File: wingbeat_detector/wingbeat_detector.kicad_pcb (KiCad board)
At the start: 4 copper layers, 36 x 18 mm, 54 parts, among them J1 USB_C_10137062-00021LF, J2 UMC_JACK_SMD, J3 UMC_JACK_SMD, J4 UMC_JACK_SMD, Q1 MOSFET-N-CH, U1 MAX865EUA+, U2 UAF42_SMA, U3 UAF42_SMA, U4 OPA381, U5 TSV630IQ1T, U6 LED_DRV_50mA

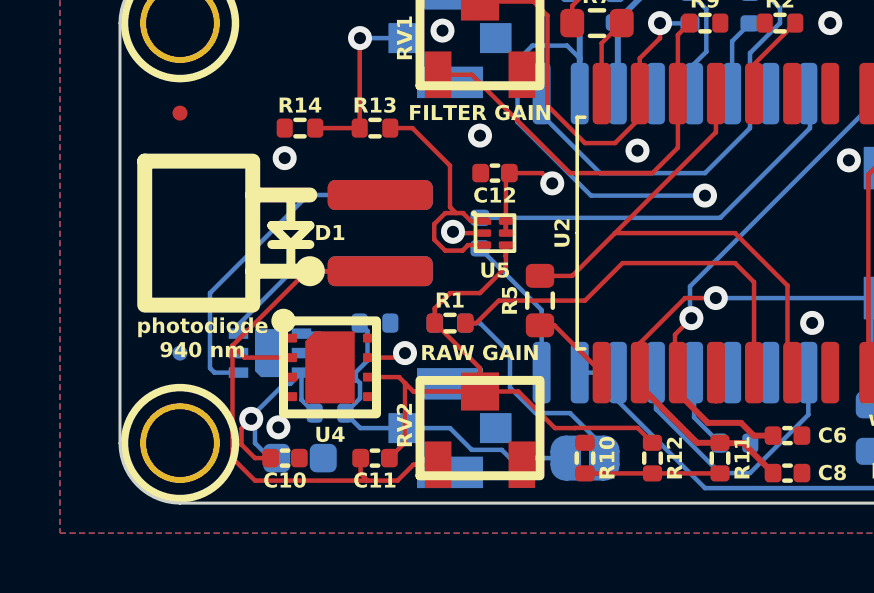
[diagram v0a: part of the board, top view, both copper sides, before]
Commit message: Remove LED
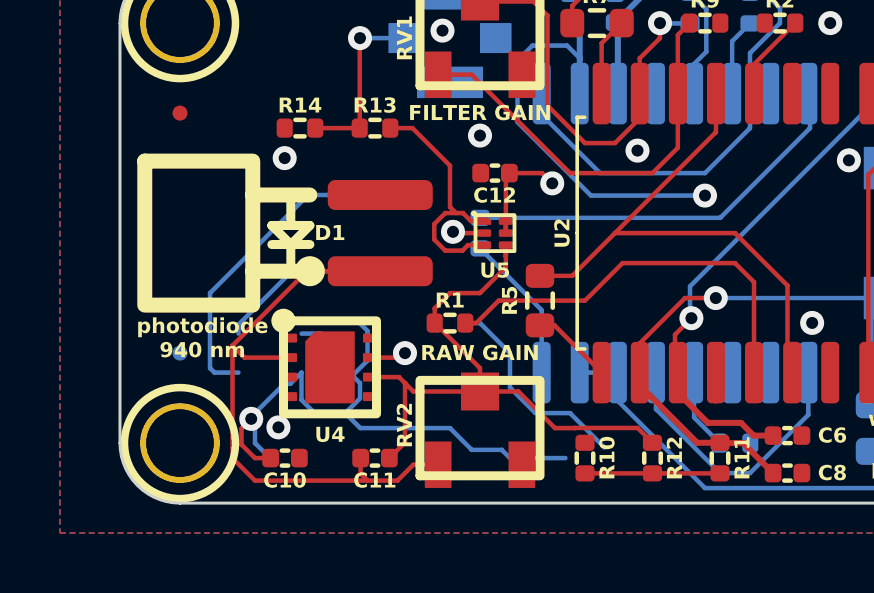
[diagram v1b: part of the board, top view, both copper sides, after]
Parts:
- removed C13: 4.7uF, Janelia:C_0603_1608Metric
- removed D2: LED, Janelia:LED_RADIAL_RA_SMD_BRIGHT
- removed J4: UMC_JACK_SMD, Janelia:UMC_AMPHENOL_A-1JB
- removed JP1: SolderJumper_2_Open, Janelia:SolderJumper-2_P1.3mm_Open_RoundedPad1.0x1.5mm
- removed Q1: MOSFET-N-CH, Janelia:XFDFN-3
- removed R15: 23.2k, Janelia:R_0402_1005Metric
- removed R16: 49.9k, Janelia:R_0402_1005Metric
- removed R17: 2k, Janelia:R_0402_1005Metric
- removed U6: LED_DRV_50mA, Janelia:DFN-6-1EP_2x2mm_P0.65mm_EP1x1.6mm
- H1, H2, H3, H4: value VAL** -> MOUNTING_HOLE_2
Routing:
- net (no net): track 0.00 -> 35.6 mm
- net /led/LED_ENABLE: track 11.5 -> 0.00 mm
- net Net-(D2-A): track 9.49 -> 0.00 mm
- net Net-(JP1-A): track 7.03 -> 0.00 mm
- net Net-(D2-K): track 5.76 -> 0.00 mm
- net /led/VB: track 1.79 -> 0.00 mm
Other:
- board text removed: "JUMP LED DEFAULT DISABLED"
- board text removed: "LED 940 nm"
- board text removed: "LED ENABLE"

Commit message: More progress towards v4
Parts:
- removed C12: 0.1uF, Janelia:C_0402_1005Metric
- removed J3: UMC_JACK_SMD, Janelia:UMC_AMPHENOL_A-1JB
- removed RV1, RV2: 500k, Janelia:Potentiometer_Bourns_3223W_Vertical
- removed U5: TSV630IQ1T, Janelia:PSON40P120X130X50-6N
- C10, C11, R11, R12, U4: moved to B.Cu
- R10: value 49.9k -> GAIN1; footprint Janelia:R_0402_1005Metric -> Janelia:R_1206_3216Metric
- R13: value 23.2k -> 49.9k; moved to B.Cu
- R14: value 49.9k -> GAIN0; footprint Janelia:R_0402_1005Metric -> Janelia:R_1206_3216Metric; moved to B.Cu
- moved R10 29.0 mm to (172.0, 92.0), turned to 180 degrees
- moved R8 17.5 mm to (155.8, 113.0)
- moved C11 13.3 mm to (139.5, 94.2)
- moved R1 13.0 mm to (142.5, 116.0)
- moved R11 12.9 mm to (139.2, 105.5), turned to 0 degrees
- moved FID1 12.1 mm to (139.0, 107.0)
- moved R5 10.9 mm to (148.8, 112.8)
- moved R12 8.49 mm to (141.5, 105.5), turned to 0 degrees
- moved R13 7.32 mm to (141.5, 103.8), turned to 0 degrees
- moved FID4 5.83 mm to (139.0, 107.0)
- moved C10 5.15 mm to (139.5, 102.8), turned to 180 degrees
- moved U4 4.50 mm to (139.5, 100.0)
- moved C1 2.00 mm to (156.0, 93.5)
- moved C2 2.00 mm to (160.0, 106.5)
- moved C3 2.00 mm to (157.5, 106.5)
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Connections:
- R10 pad 1: /GND -> Net-(U2-AAin-)
- R10 pad 2: Net-(R10-Pad2) -> /filter/HIGHPASS_AMPLIFIED
- R11 pad 1: Net-(R10-Pad2) -> /GND
- R11 pad 2: /V10- -> Net-(R11-Pad2)
- R12 pad 1: Net-(R10-Pad2) -> Net-(R11-Pad2)
- R12 pad 2: /PHOTODIODE_RAW -> /V10-
- R13 pad 1: /photodiode/PHOTODIODE_BUFFERED -> Net-(R11-Pad2)
- R13 pad 2: /photodiode/PHOTODIODE_BUFFERED_SCALED -> /PHOTODIODE_RAW
- R14 pad 1: /photodiode/PHOTODIODE_BUFFERED_SCALED -> Net-(D1-K)
- R14 pad 2: /GND -> /PHOTODIODE_RAW
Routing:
- net /V10+: track 45.3 -> 0.00 mm, vias 1 -> 0
- net /V10-: track 36.0 -> 0.00 mm, vias 2 -> 0
- net (no net): track 35.6 -> 0.00 mm
- net /filter/BANDPASS_BUFFERED: track 25.8 -> 0.00 mm
- net Net-(U2-Fadj2): track 24.5 -> 0.00 mm
- net /V5+: track 20.9 -> 0.00 mm, vias 4 -> 0
- net /PHOTODIODE_RAW: track 20.4 -> 0.00 mm
- net /filter/HIGHPASS: track 18.2 -> 0.00 mm
- net Net-(U2-AAin-): track 14.0 -> 0.00 mm
- net Net-(U3-Fadj1): track 14.0 -> 0.00 mm
- net Net-(U2-Vin1): track 13.7 -> 0.00 mm
- net Net-(U3-Fadj2): track 13.3 -> 0.00 mm
- net /filter/HIGHPASS_AMPLIFIED: track 13.0 -> 0.00 mm, vias 1 -> 0
- net Net-(D1-K): track 18.4 -> 6.29 mm, vias 0 -> 1
- net /filter/LOWPASS: track 9.39 -> 0.00 mm
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- removed copper zone on B.Cu, net /GND
- removed copper zone on F.Cu, net /GND
- removed copper zone on In1.Cu, net /GND
- removed copper zone on In2.Cu, net /V5+
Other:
- board size 36 x 18 mm -> 32 x 18 mm
- board text added: "wingbeat detector v4.0 12/2023 peter@polidoro.io"
- board text removed: "RAW OUTPUT"
- board text removed: "wingbeat detector v3.2 03/2023 peter@polidoro.io"

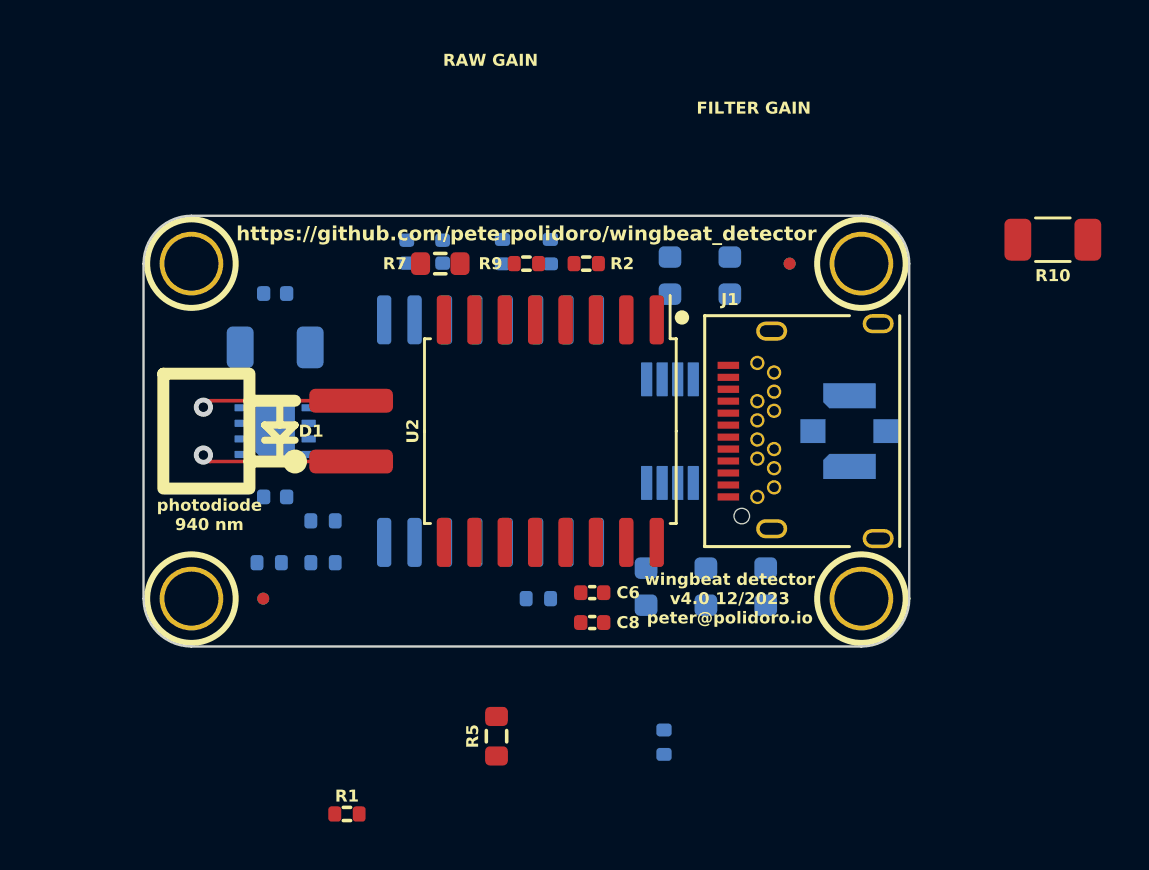
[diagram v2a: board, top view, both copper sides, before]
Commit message: First attempt at routing
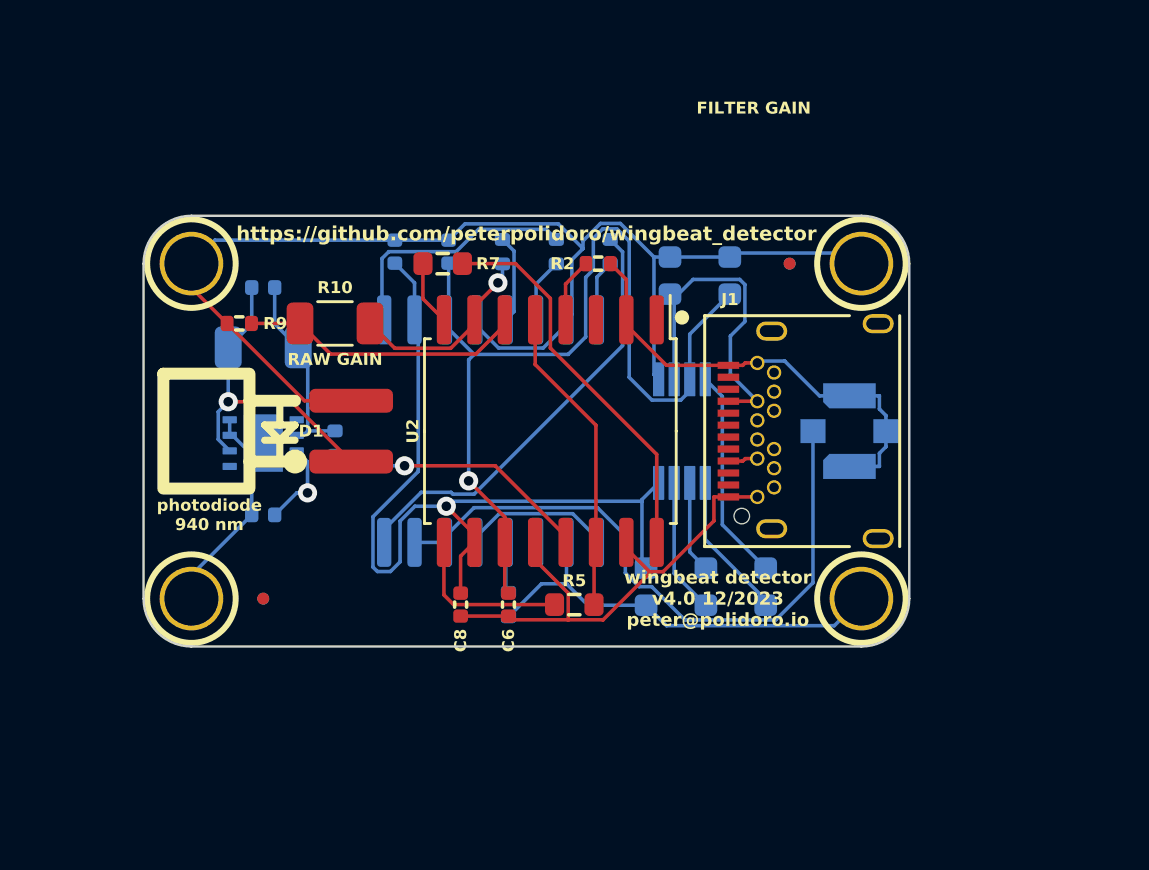
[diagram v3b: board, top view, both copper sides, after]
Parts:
- removed R12, R13: 49.9k, Janelia:R_0402_1005Metric
- removed R14: GAIN0, Janelia:R_1206_3216Metric
- C10: value 0.1uF -> 1uF
- C11: value 2pF -> 30pF
- R1: moved to B.Cu
- R11: value 49.9k -> 2M; footprint Janelia:R_0402_1005Metric -> Janelia:R_1206_3216Metric
- moved R10 30.2 mm to (142.0, 95.5), turned to 0 degrees
- moved R8 20.6 mm to (153.5, 92.5), turned to -90 degrees
- moved R1 15.5 mm to (142.0, 100.5), turned to -90 degrees
- moved R9 12.3 mm to (138.0, 95.5), turned to 180 degrees
- moved R11 9.00 mm to (139.0, 96.5)
- moved R5 6.39 mm to (152.0, 107.2), turned to 180 degrees
- moved C8 5.55 mm to (147.2, 107.2), turned to 90 degrees
- moved C6 3.54 mm to (149.2, 107.2), turned to -90 degrees
- moved R4 1.27 mm to (149.2, 107.2), turned to -90 degrees
- moved C10 0.90 mm to (139.0, 103.5)
- moved U4 0.71 mm to (139.0, 100.5)
- moved C11 0.56 mm to (139.0, 94.0)
- moved C9 0.50 mm to (144.5, 92.5)
- moved R2 0.50 mm to (153.0, 93.0), turned to 0 degrees
- moved U1 0.50 mm to (156.5, 100.0)
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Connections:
- R11 pad 1: /GND -> Net-(D1-K)
- R11 pad 2: Net-(R11-Pad2) -> /PHOTODIODE_RAW
- U4 pad 1: (no net) -> unconnected-(U4-NC-Pad1)
- U4 pad 5: (no net) -> unconnected-(U4-NC-Pad5)
- U4 pad 8: (no net) -> unconnected-(U4-NC-Pad8)
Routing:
- net /GND: track 6.29 -> 154.0 mm, vias 1 -> 0
- net /V5+: track 0.00 -> 41.1 mm, vias 0 -> 1
- net /V10+: track 0.00 -> 39.8 mm, vias 0 -> 1
- net /V10-: track 0.00 -> 35.7 mm, vias 0 -> 1
- net /filter/BANDPASS_BUFFERED: track 0.00 -> 27.2 mm
- net Net-(U3-BPVo): track 0.00 -> 18.4 mm
- net Net-(U2-Fadj2): track 0.00 -> 16.3 mm
- net /filter/HIGHPASS: track 0.00 -> 13.0 mm
- net Net-(U2-AAin-): track 0.00 -> 11.8 mm
- net Net-(U2-Vin1): track 0.00 -> 11.3 mm, vias 0 -> 1
- net Net-(U3-Fadj1): track 0.00 -> 10.6 mm
- net /power/C1+: track 0.00 -> 8.94 mm
- net /PHOTODIODE_RAW: track 0.00 -> 8.24 mm
- net /filter/HIGHPASS_AMPLIFIED: track 0.00 -> 8.23 mm, vias 0 -> 1
- net Net-(D1-K): track 6.29 -> 13.8 mm
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
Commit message: Adjust tracks and zones
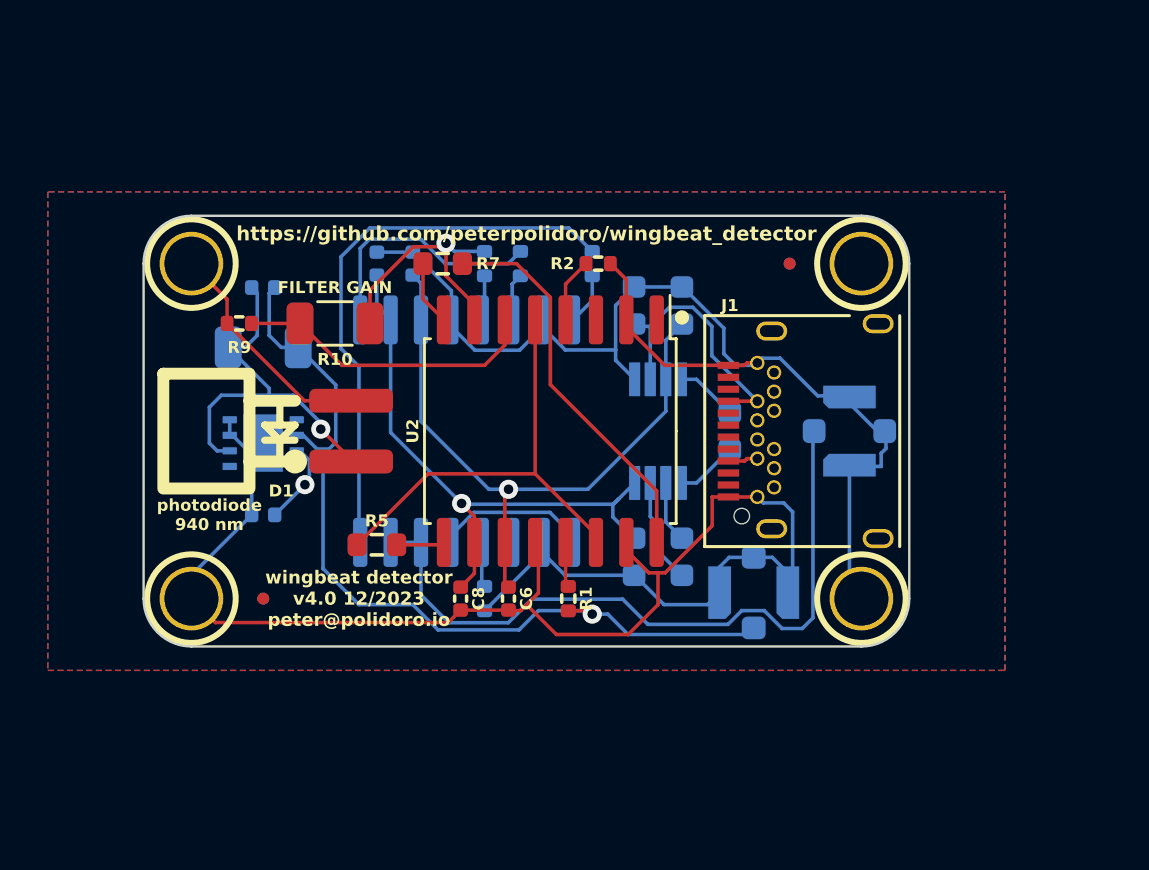
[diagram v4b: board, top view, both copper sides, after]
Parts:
- added J3: UMC_JACK_SMD, Janelia:UMC_AMPHENOL_A-1JB, B.Cu at (159.5, 106.8)
- R1: moved to F.Cu
- moved R1 11.7 mm to (151.8, 107.0), turned to 90 degrees
- moved R5 8.62 mm to (143.8, 104.8), turned to 0 degrees
- moved C2 6.67 mm to (158.5, 100.0)
- moved C4 2.36 mm to (156.5, 94.8)
- moved C1 1.95 mm to (154.5, 94.8)
- moved C3 1.60 mm to (156.5, 105.2)
- moved C7 1.58 mm to (145.2, 93.0)
- moved R6 1.58 mm to (149.8, 93.0)
- moved C5 1.35 mm to (154.5, 105.2)
- moved R4 1.03 mm to (148.2, 107.0)
- moved U1 1.00 mm to (155.5, 100.0)
- moved U3 1.00 mm to (147.5, 100.0)
- moved C9 0.90 mm to (143.8, 93.0)
- moved R3 0.90 mm to (148.2, 93.0), turned to -90 degrees
- moved R8 0.90 mm to (152.8, 93.0)
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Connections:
- net /PHOTODIODE_RAW renamed /PHOTODIODE_SIG
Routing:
- net /PHOTODIODE_SIG: track 8.24 -> 36.2 mm, vias 0 -> 1
- net /V10+: track 39.8 -> 27.3 mm
- net /V10-: track 35.7 -> 24.7 mm
- net Net-(U2-Vin1): track 11.3 -> 1.89 mm, vias 1 -> 0
- net /power/C1+: track 8.94 -> 2.60 mm
- net /filter/HIGHPASS: track 13.0 -> 19.0 mm
- net Net-(U3-BPVo): track 18.4 -> 23.7 mm
- net Net-(U2-Fadj1): track 6.99 -> 2.02 mm
- net /GND: track 154.0 -> 158.9 mm
- net /power/C1-: track 6.16 -> 2.60 mm
- net /V5+: track 41.1 -> 38.6 mm
- net /filter/HIGHPASS_AMPLIFIED: track 8.23 -> 10.8 mm
- net /filter/BANDPASS_BUFFERED: track 27.2 -> 29.7 mm
- net Net-(D1-K): track 13.8 -> 16.2 mm
- net Net-(U3-Vin1): track 3.70 -> 1.89 mm
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- added copper zone on B.Cu, net /GND
- added copper zone on F.Cu, net /GND
- added copper zone on In1.Cu, net /GND
- added copper zone on In2.Cu, net /V5+
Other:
- board text added: "DIODE GAIN"
- board text added: "FILTERED OUTPUT"
- board text removed: "FILTER OUTPUT"
- board text removed: "RAW GAIN"

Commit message: Rearrange parts
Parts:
- J3: moved to F.Cu
- moved J3 17.6 mm to (142.0, 105.0), turned to 90 degrees
- moved FID2 14.0 mm to (160.0, 107.0)
- moved FID4 14.0 mm to (140.0, 93.0)
- moved R5 10.0 mm to (153.5, 107.0), turned to 180 degrees
- moved C11 9.01 mm to (139.5, 103.0), turned to 180 degrees
- moved C10 6.52 mm to (139.5, 97.0)
- moved R11 4.61 mm to (136.0, 100.0), turned to 90 degrees
- moved R9 4.12 mm to (142.0, 96.5), turned to 0 degrees
- moved C6 1.25 mm to (148.0, 107.0)
- moved R10 1.00 mm to (142.0, 94.5)
- moved C8 0.75 mm to (146.5, 107.0)
- moved R1 0.75 mm to (151.0, 107.0)
- moved U4 0.71 mm to (139.5, 100.0), turned to 90 degrees
- moved FID3 0.25 mm to (161.2, 93.0)
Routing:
- net Net-(U2-Fadj1): track 2.02 -> 11.9 mm
- net /PHOTODIODE_SIG: track 36.2 -> 28.3 mm
- net /GND: track 158.9 -> 151.5 mm
- net Net-(D1-K): track 16.2 -> 9.09 mm
- net /filter/HIGHPASS: track 19.0 -> 13.3 mm
- net /filter/BANDPASS_BUFFERED: track 29.7 -> 25.1 mm
- net /V10+: track 27.3 -> 25.5 mm
- net Net-(U2-AAin-): track 12.7 -> 11.0 mm
- net /filter/HIGHPASS_AMPLIFIED: track 10.8 -> 9.82 mm
- net /V5+: track 38.6 -> 37.9 mm
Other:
- board text added: "DIODE TEST POINT"

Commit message: Update images and documentation
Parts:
- R10: value GAIN1 -> 150k
- moved R11 0.25 mm to (136.2, 100.0)
